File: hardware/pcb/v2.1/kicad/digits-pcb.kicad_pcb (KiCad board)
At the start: 2 copper layers, 76.2 x 61.9 mm, 71 parts, among them J1 Conn_02x20_Odd_Even, J3 VIN_BARREL_PIGTAIL, J4 Conn_01x07, J6 Conn_01x02, J7 Screw_Terminal_01x02, J8 Conn_01x04, J9 Conn_01x03, SW1 SW_Push, U1 LM2596S-5, U2 DRV8871DDAR, U3 RP2040, U4 W25Q16JVSSIQ, U5 AMS1117-3.3, U6 TLV320AIC3104IRHBR, U7 XC6206P182MR, Y1 ABM8-272-T3

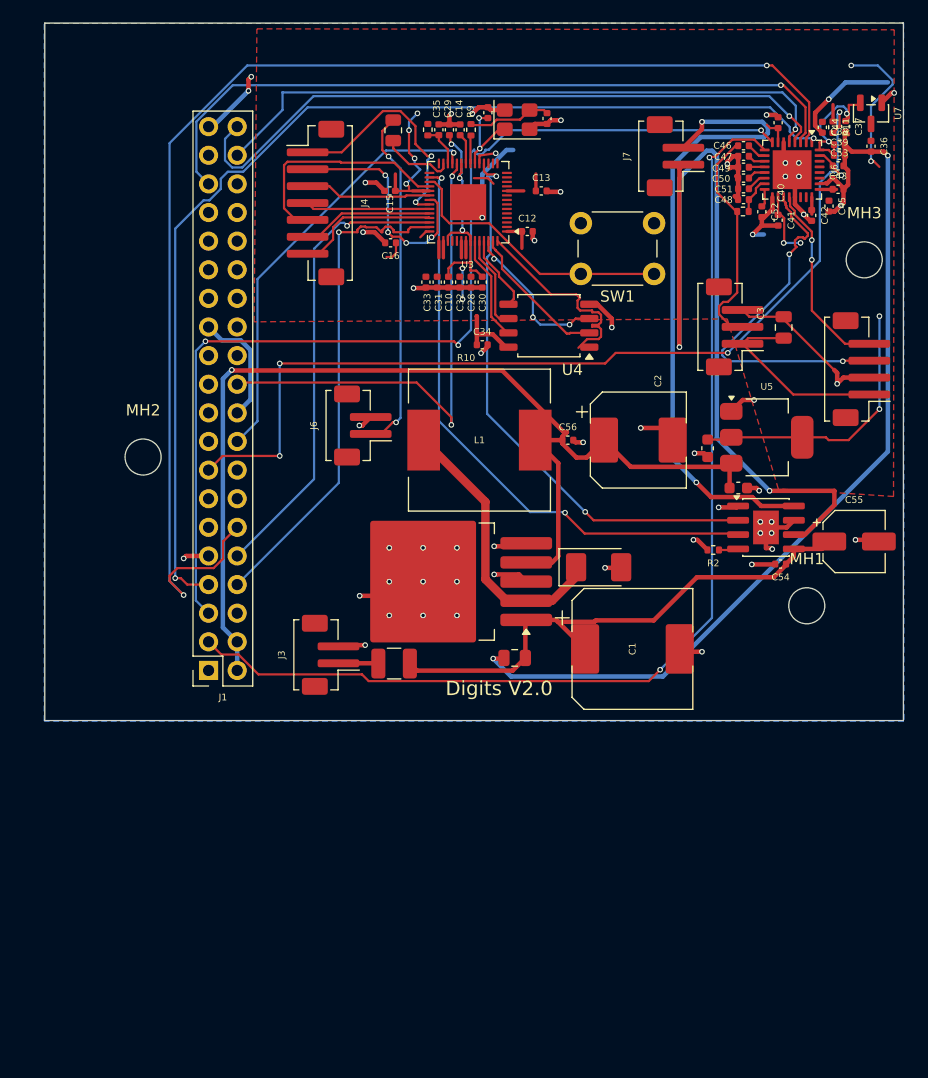
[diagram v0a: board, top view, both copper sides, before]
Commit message: fix(hardware): swap J6 LED polarity and place SW2 on PCB v2.1 (#322)
J6 pin 1 and pin 2 net assignments are swapped so the stock donor-phone
LED cable plugs in directly without per-unit crimp rework. Pin 1 is now
GND, pin 2 is LED_A. See hardware/pcb/v2/ERRATA.md section 8 for the
underlying defect.

SW2 (BOOTSEL tact switch) was already in the v2.1 schematic but had no
PCB placement. Placed on the carrier with QSPI_SS and GND routed clean,
labeled BOOTSEL on the silkscreen.

DRC: 0 errors, 0 unconnected items. Remaining warnings are pre-existing
silkscreen overlap and library-footprint drift carried over from main.
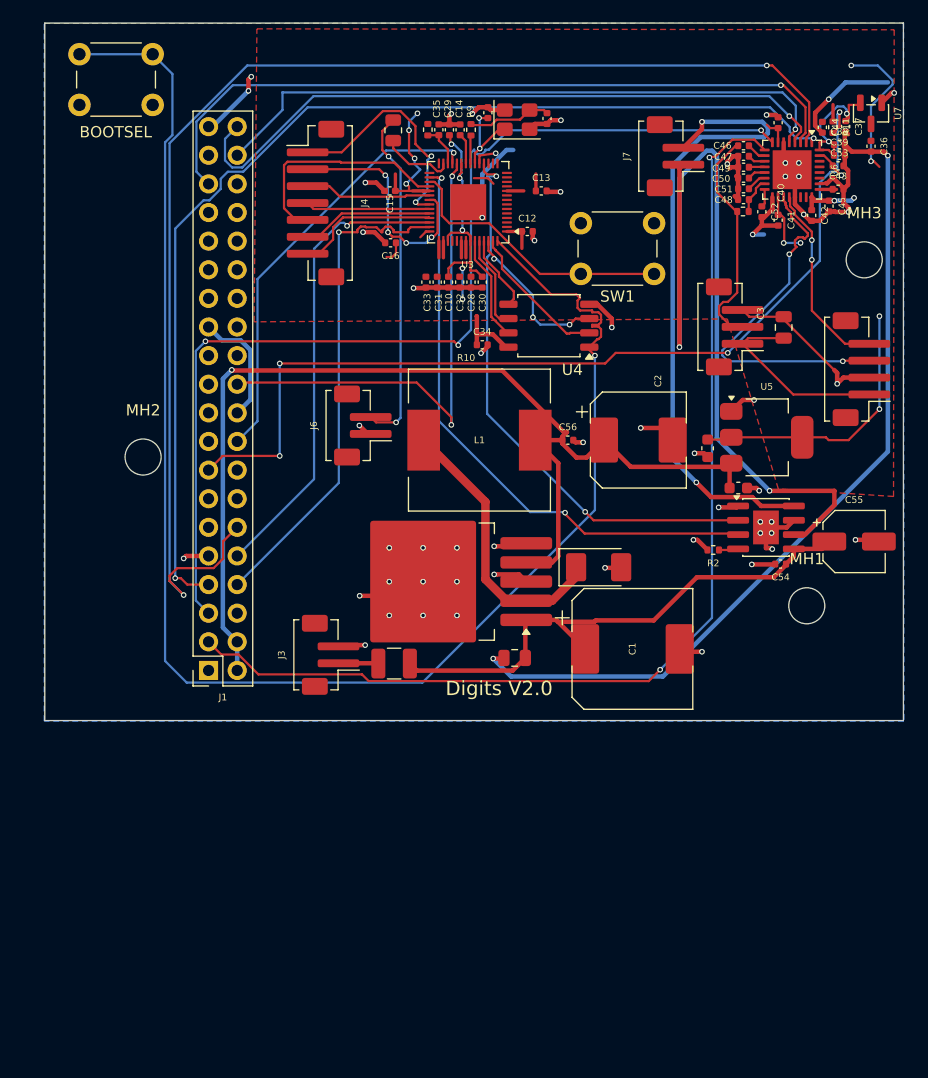
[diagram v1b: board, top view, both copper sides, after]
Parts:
- added SW2: SW_Push, Button_Switch_THT:SW_PUSH_6mm, F.Cu at (17.8, 12.2)
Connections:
- J6 pad 1: LED_A -> GND
- J6 pad 2: GND -> LED_A
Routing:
- net QSPI_SS: track 18.5 -> 138.8 mm, vias 0 -> 1
- net +3V3: track 94.3 -> 97.9 mm, vias 12 -> 14
- net GND: track 233.5 -> 236.0 mm
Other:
- board text added: "BOOTSEL"

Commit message: feat(hardware): integrate DPDT hook switch and on-board boost converter into PCB v2.1
Two architectural changes consolidated into v2.1 (previously scoped for v3):

1. DPDT hook switch replaces SW1 (tact switch) and J9 (mic kill JST connector).
   Single 6-pin telephone hook switch (IL Switch 2240 / Innocent INH-2240 family)
   provides both hook sense and mic kill from one mechanical actuation. Lifting
   the handset both signals off-hook and connects the microphone to the codec.
   Eliminates J9 connector and its external microswitch harness.

2. XL6019 boost converter (12V to 42V) replaces the external mains transformer.
   Feeds the DRV8871 H-bridge VM pin so the bell sees 84Vpp drive instead of
   24Vpp. At ~4k coil impedance the bell ringer gets ~12x the power of direct
   12V drive, roughly halfway to transformer-level loudness on the perceptual
   scale. Eliminates the external 120V/12V transformer and its flying wires.
   J7 stays as the bell coil output.

Components added:
- SW1: SW_DPDT_x2 with custom 24.2x17.1mm footprint (5mm pin pitch, 7.75mm
  row spacing, 0.9mm signal pin / 2.1mm mounting pin)
- U10: XLSEMI XL6019E1 boost IC (LCSC C73018, TO-263-5)
- L10: 47uH/4.6A shielded power inductor (LCSC C9906, 12.3x12.3mm)
- D10: SS56 60V/5A Schottky diode (LCSC C65009, SMA)
- C100: 100uF/63V SMD electrolytic output cap (LCSC C28241, 10mm dia)
- C101: 1uF/100V 0805 ceramic output cap
- R20/R21: 64.9k/2k 0402 feedback divider (sets VBOOST to 41.8V)

Components removed:
- SW1 (2-pin 6mm tact switch)
- J9 (3-pin JST ZH mic kill connector)

LCSC-sourced symbols and footprints pulled via easyeda2kicad, registered
through sym-lib-table and fp-lib-table.

Schematic notes:
- VBOOST is a local net in the ringer sub-sheet; PWR_FLAG marks it as driven
- LCSC XL6019 symbol mislabels pin 6 (thermal tab) as SW; overridden with GND
  label in schematic to match the datasheet
- New refs (U10, L10, D10, C100, C101, R20, R21) chosen to avoid collisions
  with existing parent-sh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
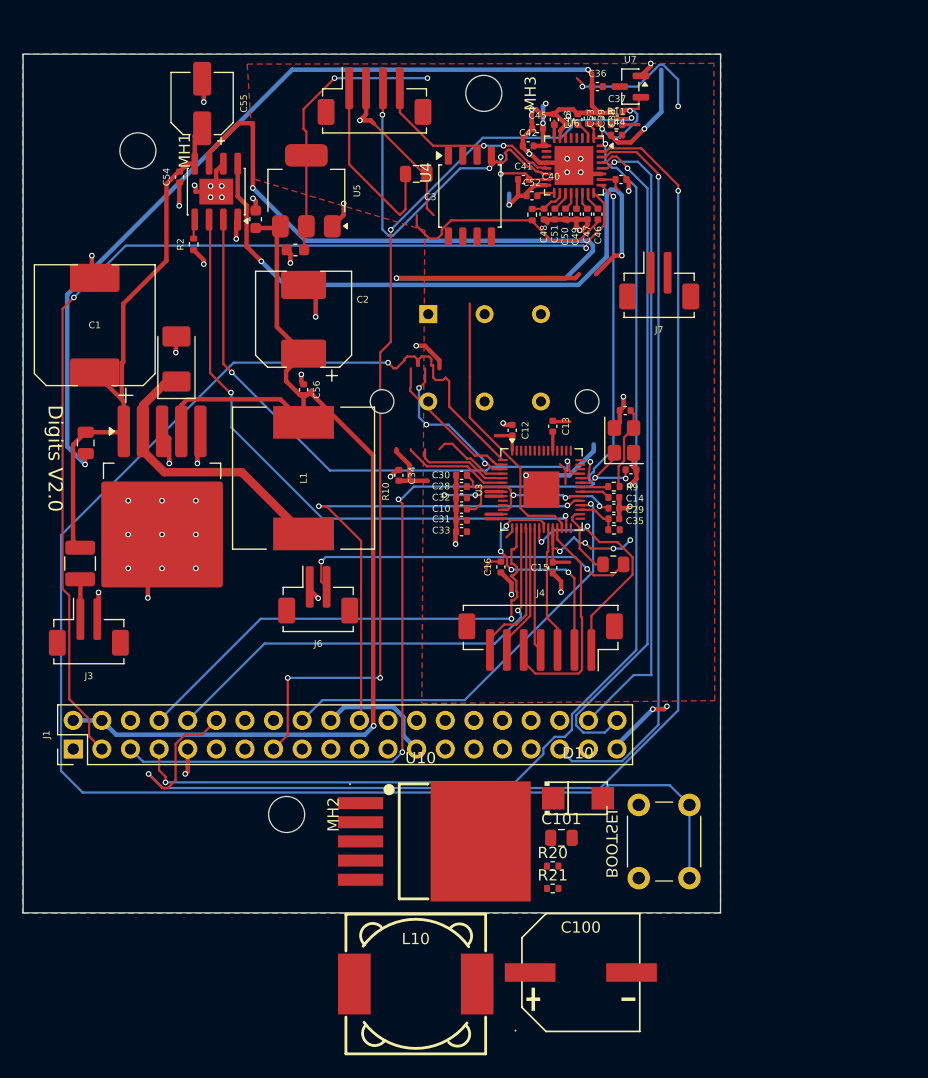
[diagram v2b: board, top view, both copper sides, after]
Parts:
- removed J9: Conn_01x03, Connector_JST:JST_ZH_B3B-ZR-SM4-TF_1x03-1MP_P1.50mm_Vertical
- added C100: 100uF, cap-out-lcsc:CAP-SMD_BD10.0-L10.3-W10.3-FD, F.Cu at (62.2, 93.7)
- added C101: 1uF, Capacitor_SMD:C_0805_2012Metric, F.Cu at (60.5, 81.8)
- added D10: SS56, ss56-lcsc:SMA_L4.3-W2.6-LS5.2-RD, F.Cu at (62.0, 78.2)
- added L10: 47uH, inductor-lcsc:IND-SMD_L12.3-W12.3, F.Cu at (47.6, 94.7)
- added R20: 64.9k, Resistor_SMD:R_0402_1005Metric, F.Cu at (59.8, 84.3)
- added R21: 2k, Resistor_SMD:R_0402_1005Metric, F.Cu at (59.8, 86.2)
- added U10: XL6019E1, xl6019:TO-263-5_L10.2-W9.9-P1.70-LS14.4-TL, F.Cu at (48.0, 82.1)
- SW1: value SW_Push -> Hook_DPDT; footprint Button_Switch_THT:SW_PUSH_6mm -> digits-pcb:SW_DPDT_Hook_24.2x17.1mm
- moved SW2 91.0 mm to (71.9, 85.3), turned to 90 degrees
- moved MH1 71.8 mm to (22.9, 20.8), turned to 90 degrees
- moved C55 69.7 mm to (28.6, 16.6), turned to 90 degrees
- moved C54 63.4 mm to (26.6, 23.1), turned to -90 degrees
- moved U2 57.2 mm to (29.9, 24.4), turned to 90 degrees
- moved C1 55.7 mm to (19.1, 36.3), turned to 90 degrees
- moved R2 53.5 mm to (27.9, 29.1), turned to -90 degrees
- moved J8 49.5 mm to (43.9, 15.9), turned to 0 degrees
- moved C11 49.0 mm to (33.4, 26.9), turned to 90 degrees
- moved U5 46.3 mm to (37.9, 24.3), turned to 90 degrees
- moved J4 43.8 mm to (58.7, 64.4), turned to 180 degrees
- moved R1 43.2 mm to (65.1, 57.5), turned to 0 degrees
- moved C4 42.6 mm to (18.3, 46.7), turned to -90 degrees
- moved D1 41.8 mm to (26.4, 39.3), turned to 90 degrees
- moved C9 40.6 mm to (36.9, 29.6), turned to 180 degrees
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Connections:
- SW1 pad 1: HOOK_SW -> unconnected-(SW1A-A-Pad1)
- SW1 pad 2: GND -> HOOK_SW
- U2 pad 5: +12V -> /ringer/VBOOST
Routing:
- net +3V3: track 97.9 -> 96.4 mm
- net GND: track 236.0 -> 236.2 mm, vias 59 -> 58
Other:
- board size 76.2 x 61.9 mm -> 61.9 x 76.2 mm

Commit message: feat(hardware): switch to 5V input, drop buck stage, retarget boost to 37V
Bench testing confirmed the on-board boost approach matches the external
transformer for bell loudness: 79 dBA (transformer) vs 78 dBA (boost at 33V),
measured same distance/room/meter. The transformer is no longer justified.

Power input changed from 12V to 5V:
- Removed the entire LM2596 buck stage (U1, L1, D1, C2, C56). With 5V input
  there is nothing to buck down for the Pi; 5V feeds the Pi, the AMS1117 LDO,
  and the XL6019 boost directly.
- Merged the old +12V rail into +5V throughout both sheets.
- J3 connector kept as-is for now (barrel-jack pigtail); it will need a
  higher-current part since 5V at the same power draws ~2x the current.
- R12 (12V power LED resistor) changed 1k -> 300R to rebias for the 5V rail.

Boost output retargeted 42V -> 37V (R20 64.9k -> 57.6k, R21 unchanged at 2k):
- 37V gives 8V margin below the DRV8871's 45V VM limit (was only 3V at 42V).
- Bell already measured 78 dBA at 33V; 37V is marginally louder with far
  better headroom against inductive-kickback spikes.
- Lower boost ratio is also easier on the XL6019 from a 5V input.

PCB: boost cluster (U10/L10/D10/C100/C101/R20/R21) repositioned from the
off-board scratch area into the region between U2 and the codec. All
footprints on F.Cu. Layout and routing still in progress.

ERC clean (0 errors). Netlist: 77 components, +12V net fully eliminated,
codec subsheet intact (22 components).
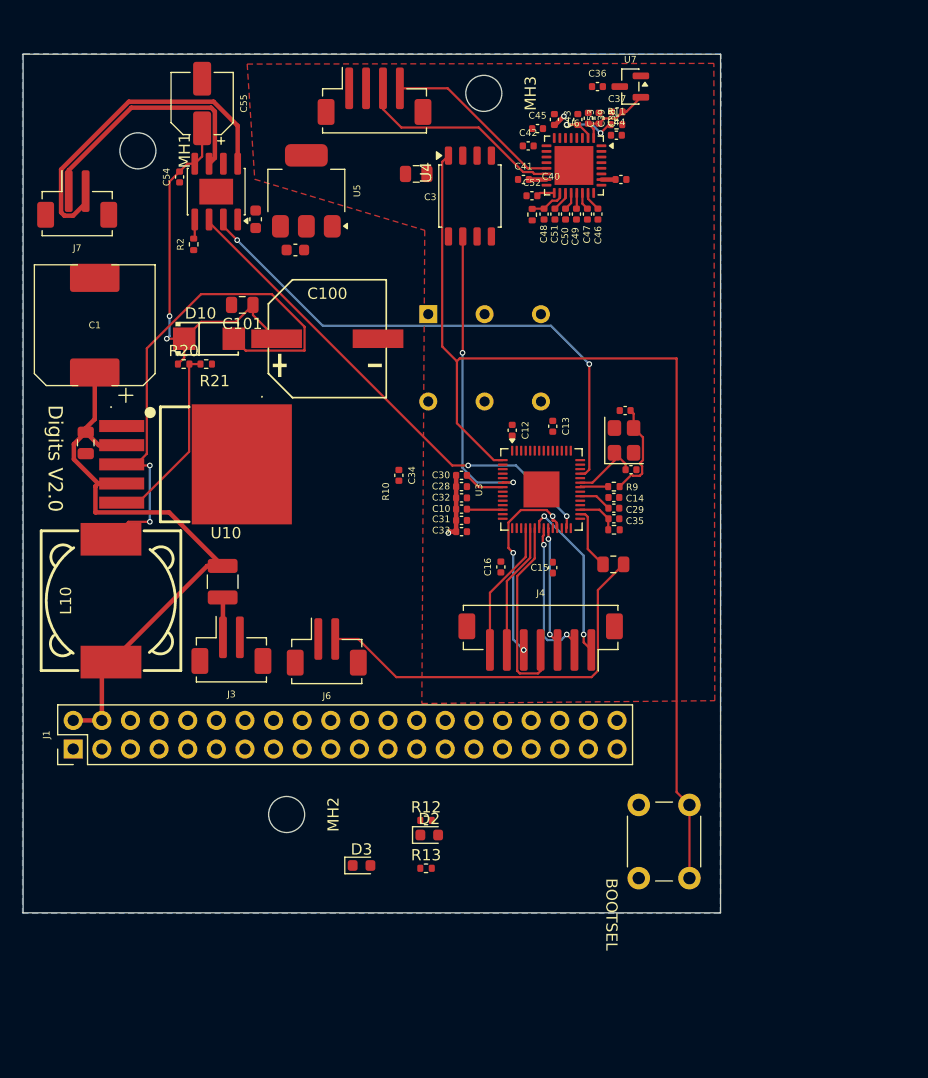
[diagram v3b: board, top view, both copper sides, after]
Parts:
- removed C2: 220uF, Capacitor_SMD:CP_Elec_8x6.5
- removed C56: 100nF, Capacitor_SMD:C_0402_1005Metric
- removed D1: SS54, Diode_SMD:D_SMA
- removed L1: 33uH, Inductor_SMD:L_12x12mm_H8mm
- removed U1: LM2596S-5, Package_TO_SOT_SMD:TO-263-5_TabPin3
- added D2: LED_RED, LED_SMD:LED_0603_1608Metric, F.Cu at (48.8, 81.5)
- added D3: LED_GREEN, LED_SMD:LED_0603_1608Metric, F.Cu at (42.8, 84.2)
- added R12: 300, Resistor_SMD:R_0402_1005Metric, F.Cu at (48.5, 80.2)
- added R13: 330, Resistor_SMD:R_0402_1005Metric, F.Cu at (48.5, 84.5)
- moved C100 60.6 mm to (39.8, 37.5)
- moved R21 55.8 mm to (29.0, 39.7)
- moved R20 55.3 mm to (27.0, 39.7)
- moved C101 55.1 mm to (32.2, 34.5), turned to 180 degrees
- moved D10 52.3 mm to (29.2, 37.5)
- moved J7 52.2 mm to (17.6, 25.1)
- moved L10 43.5 mm to (20.6, 60.7), turned to 90 degrees
- moved U10 39.6 mm to (26.8, 48.6)
- moved F1 12.8 mm to (30.5, 59.0)
- moved J3 12.8 mm to (31.2, 64.7)
- moved J6 4.69 mm to (39.7, 64.8)
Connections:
- C1 pad 1: +12V -> +5V
- C4 pad 1: +12V -> +5V
- C54 pad 1: +12V -> /ringer/VBOOST
- C55 pad 1: +12V -> /ringer/VBOOST
- F1 pad 2: +12V -> +5V
- L10 pad 1: +12V -> +5V
- U10 pad 2: +12V -> +5V
- U10 pad 4: +12V -> +5V
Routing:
- net GND: track 236.2 -> 5.73 mm, vias 58 -> 1
- net CODEC_BCLK: track 116.2 -> 0.00 mm, vias 2 -> 0
- net CODEC_MCLK: track 97.7 -> 0.00 mm, vias 2 -> 0
- net CODEC_SDA: track 95.3 -> 0.00 mm, vias 2 -> 0
- net CODEC_SCL: track 93.6 -> 0.00 mm, vias 3 -> 0
- net +3V3: track 96.4 -> 3.99 mm, vias 14 -> 1
- net CODEC_RESET: track 86.4 -> 7.11 mm, vias 5 -> 2
- net CODEC_WCLK: track 65.5 -> 0.00 mm, vias 1 -> 0
- net CODEC_DIN: track 60.1 -> 0.00 mm, vias 1 -> 0
- net BELL_A: track 79.3 -> 22.1 mm, vias 2 -> 0
- net CODEC_DOUT: track 56.8 -> 0.00 mm, vias 1 -> 0
- net /ringer/SW_NODE: track 0.00 -> 49.6 mm, vias 0 -> 2
- net +12V: track 48.1 -> 0.00 mm
- net UART_TX_PI: track 44.6 -> 0.00 mm, vias 1 -> 0
- net SWD_SWCLK: track 44.4 -> 0.00 mm, vias 2 -> 0
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
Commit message: chore(hardware): sync PCB to corrected schematic (LCSC fields, U10 tab on SW_NODE)
Checkpoint of the board after Update PCB from Schematic. The PCB now reflects
all recent schematic work: buck stage footprints removed (U1/L1/D1/C2/C56),
power LED footprints added (D2/D3/R12/R13), boost cluster present, LCSC part
numbers propagated onto footprints for the BOM, and crucially U10 pad 6 (the
XL6019 metal tab) now carries net SW_NODE instead of GND - matching the tab=SW
datasheet fix. 77 footprints, balanced, ERC-clean schematic source.

Layout/routing still pending (task 6): nets are assigned but most are
unrouted. The U10 tab copper must be pulled off the GND pour onto a modest
SW_NODE island during routing; DRC will flag it as a GND-zone intrusion until
then, which is the intended reminder.
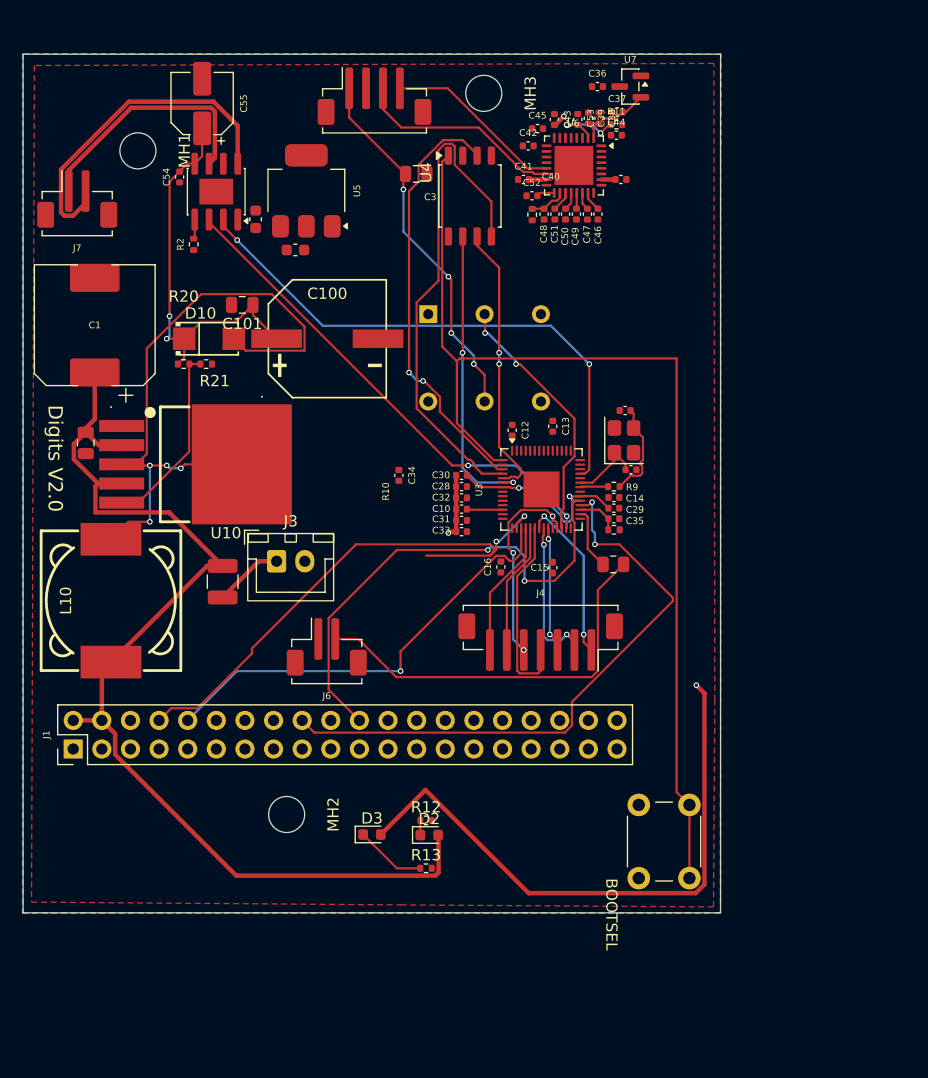
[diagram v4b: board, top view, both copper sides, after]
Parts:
- J3: footprint Connector_JST:JST_ZH_B2B-ZR-SM4-TF_1x02-1MP_P1.50mm_Vertical -> Connector_JST:JST_XH_B2B-XH-A_1x02_P2.50mm_Vertical
- R20: value 64.9k -> 57.6k
- moved J3 8.46 mm to (35.2, 57.2)
- moved D3 2.90 mm to (43.7, 81.5)
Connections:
- U10 pad 6: GND -> /ringer/SW_NODE
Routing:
- net SWD_SWDIO: track 0.00 -> 53.6 mm, vias 0 -> 2
- net +3V3: track 3.99 -> 56.4 mm, vias 1 -> 2
- net UART_TX_PI: track 0.00 -> 49.4 mm, vias 0 -> 2
- net QSPI_SD0: track 0.00 -> 45.0 mm
- net SWD_SWCLK: track 0.00 -> 43.8 mm, vias 0 -> 2
- net +5V: track 54.7 -> 94.8 mm
- net UART_RX_PI: track 0.00 -> 39.4 mm, vias 0 -> 1
- net QSPI_SD2: track 0.00 -> 38.2 mm, vias 0 -> 2
- net MIC_HOT: track 0.00 -> 32.9 mm, vias 0 -> 4
- net QSPI_SCLK: track 0.00 -> 24.6 mm, vias 0 -> 2
- net HOOK_SW: track 0.00 -> 23.2 mm, vias 0 -> 2
- net DVDD_1V1: track 9.83 -> 20.6 mm, vias 0 -> 2
- net /ringer/SW_NODE: track 49.6 -> 58.0 mm, vias 2 -> 4
- net /LED3V3_K: track 0.00 -> 6.32 mm
- net /VIN_RAW: track 3.55 -> 6.12 mm
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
